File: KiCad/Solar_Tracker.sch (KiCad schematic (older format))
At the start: 127 parts

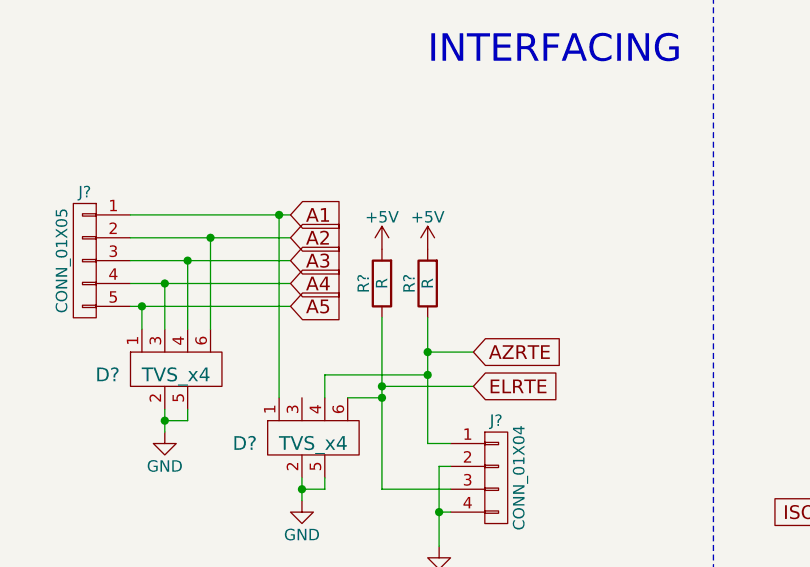
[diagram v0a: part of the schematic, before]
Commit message: Updated pullups on config jumpers
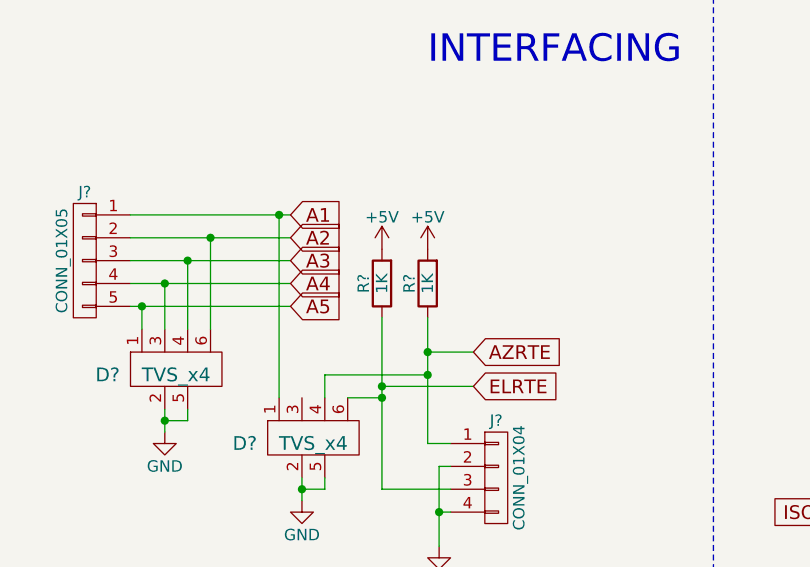
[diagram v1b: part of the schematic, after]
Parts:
- R? (x2): value R -> 1K
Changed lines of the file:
@@
 P 8300 6100
 F 0 "R?" V 8380 6100 50  0000 C CNN
-F 1 "R" V 8300 6100 50  0000 C CNN
+F 1 "1K" V 8300 6100 50  0000 C CNN
 F 2 "" V 8230 6100 50  0001 C CNN
 F 3 "" H 8300 6100 50  0001 C CNN
@@
 P 8500 6100
 F 0 "R?" V 8580 6100 50  0000 C CNN
-F 1 "R" V 8500 6100 50  0000 C CNN
+F 1 "1K" V 8500 6100 50  0000 C CNN
 F 2 "" V 8430 6100 50  0001 C CNN
 F 3 "" H 8500 6100 50  0001 C CNN

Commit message: Annotated
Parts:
- gave numbers to parts that had none: 127

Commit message: Redid analog connector
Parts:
- removed D6: TVS_x4, symbol TVS_x4
- removed J6, J7: CONN_01X04, symbol CONN_01X04
- added D14: TVS_x4, symbol TVS_x4
- added J10, J11, J12, J13: HOLE, symbol CONN_01X01
- added J14: ELJMP, symbol CONN_01X02_MALE
- added J6: GPIO, symbol CONN_01X08
- added J7: AZJMP, symbol CONN_01X02_MALE
- added R44: 150, symbol R
- R15, R26, R43, R7: value R -> 1K
- renumbered D14 to D6
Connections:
- net +5V: now also R44.2
- net A0: now also D7.3, J4.2 (P2)
- net A1: now also J4.3 (P3); no longer J4.1 (P1)
- net A2: now also D14.6, J6.5 (P5); no longer J4.2 (P2)
- net A3: now also D14.4, J6.6 (P6); no longer J4.3 (P3)
- net A4: now also D14.3, J6.7 (P7); no longer J4.4 (P4)
- net A5: now also D14.1, J6.8 (P8); no longer J4.5 (P5)
- net AZRTE: now also J7.1
- net D4: now also J6.1 (P1)
- net D5: now also J6.2 (P2)
- net D6: now also J6.3 (P3)
- net D7: now also J6.4 (P4)
- net ELRTE: now also J14.1
- net Earth: now also C1.2, C10.2, C11.2, C12.2, C13.2, C14.2, C15.2, C16.2, C2.2, C20.2, C21.2, C26.2, C28.2, C29.2, C3.2, C4.2, C6.2, C9.2, D2.3 (GND), D7.2, D7.5, D8.2, D8.5, D9.2, D9.5, J1.2 (Pin_2), J2.5 (GND), J2.6 (Shield), J4.4 (P4), J4.5 (P5), J5.6 (P6), R1.2, R12.2, R18.2, R25.2, R27.2, R32.2, R8.2, R9.2, SW1.~, U1.2 (-Vin), U1.4 (-Vout), U10.2, U12.1 (GND), U12.P (PAD), U2.1 (GND), U2.P (PAD), U3.15 (GND), U3.23 (GND), U3.35 (GND), U3.43 (GND), U3.5 (UGND), U4.1 (GND), U4.P (PAD), U5.1 (GND), U5.P (PAD), U6.2 (-Vin), U7.3, U8.3, U9.2, Y1.2, D14.2, D14.5, J10.1 (P1), J11.1 (P1), J12.1 (P1), J13.1 (P1), J14.2, J7.2
- removed net GND: C1.2, C10.2, C11.2, C12.2, C13.2, C14.2, C15.2, C16.2, C2.2, C20.2, C21.2, C26.2, C28.2, C29.2, C3.2, C4.2, C6.2, C9.2, D2.3 (GND), D7.2, D7.5, D8.2, D8.5, D9.2, D9.5, J1.2 (Pin_2), J2.5 (GND), J2.6 (Shield), J5.6 (P6), R1.2, R12.2, R18.2, R25.2, R27.2, R32.2, R8.2, R9.2, SW1.~, U1.2 (-Vin), U1.4 (-Vout), U10.2, U12.1 (GND), U12.P (PAD), U2.1 (GND), U2.P (PAD), U3.15 (GND), U3.23 (GND), U3.35 (GND), U3.43 (GND), U3.5 (UGND), U4.1 (GND), U4.P (PAD), U5.1 (GND), U5.P (PAD), U6.2 (-Vin), U7.3, U8.3, U9.2, Y1.2
- new net: J4.1 (P1), R44.1
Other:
- note added: "BLK"
- note added: "BRE"
- note added: "GRN"
- note added: "RED"
- note added: "WHT"
- moved on the sheet: D7, D9

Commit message: New motor cap values
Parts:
- C15, C20, C28, C3: value 560nF?? -> 1u
- C16, C17, C21, C22, C29, C31, C4, C5: value 100nF -> 100n
- C18, C23, C33, C7: value 12nF????? -> 0.015u
- C19, C24, C36, C8: value 470nF -> 470n
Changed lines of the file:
@@
 P 14950 3100
 F 0 "C33" H 14960 3170 50  0000 L CNN
-F 1 "12nF?????" H 14850 3050 50  0000 L CNN
+F 1 "0.015u" H 14850 3050 50  0000 L CNN
 F 2 "" H 14950 3100 50  0001 C CNN
 F 3 "" H 14950 3100 50  0001 C CNN
@@
 P 14150 1100
 F 0 "C29" H 14160 1170 50  0000 L CNN
-F 1 "100nF" H 14050 1050 50  0000 L CNN
+F 1 "100n" H 14050 1050 50  0000 L CNN
 F 2 "" H 14150 1100 50  0001 C CNN
 F 3 "" H 14150 1100 50  0001 C CNN
@@
 P 15850 2100
 F 0 "C36" H 15860 2170 50  0000 L CNN
-F 1 "470nF" H 15750 2050 50  0000 L CNN
+F 1 "470n" H 15750 2050 50  0000 L CNN
 F 2 "" H 15850 2100 50  0001 C CNN
 F 3 "" H 15850 2100 50  0001 C CNN
@@
 P 14150 750
 F 0 "C28" H 14160 820 50  0000 L CNN
-F 1 "560nF??" H 14050 700 50  0000 L CNN
+F 1 "1u" H 14050 700 50  0000 L CNN
 F 2 "" H 14150 750 50  0001 C CNN
 F 3 "" H 14150 750 50  0001 C CNN
@@
 P 14400 3300
 F 0 "C31" H 14410 3370 50  0000 L CNN
-F 1 "100nF" H 14410 3220 50  0000 L CNN
+F 1 "100n" H 14410 3220 50  0000 L CNN
 F 2 "" H 14400 3300 50  0001 C CNN
 F 3 "" H 14400 3300 50  0001 C CNN
@@
 P 10900 3100
 F 0 "C23" H 10910 3170 50  0000 L CNN
-F 1 "12nF?????" H 10800 3050 50  0000 L CNN
+F 1 "0.015u" H 10800 3050 50  0000 L CNN
 F 2 "" H 10900 3100 50  0001 C CNN
 F 3 "" H 10900 3100 50  0001 C CNN
@@
 P 10100 1100
 F 0 "C21" H 10110 1170 50  0000 L CNN
-F 1 "100nF" H 10000 1050 50  0000 L CNN
+F 1 "100n" H 10000 1050 50  0000 L CNN
 F 2 "" H 10100 1100 50  0001 C CNN
 F 3 "" H 10100 1100 50  0001 C CNN
@@
 P 11800 2100
 F 0 "C24" H 11810 2170 50  0000 L CNN
-F 1 "470nF" H 11700 2050 50  0000 L CNN
+F 1 "470n" H 11700 2050 50  0000 L CNN
 F 2 "" H 11800 2100 50  0001 C CNN
 F 3 "" H 11800 2100 50  0001 C CNN
@@
 P 10100 750
 F 0 "C20" H 10110 820 50  0000 L CNN
-F 1 "560nF??" H 10000 700 50  0000 L CNN
+F 1 "1u" H 10000 700 50  0000 L CNN
 F 2 "" H 10100 750 50  0001 C CNN
 F 3 "" H 10100 750 50  0001 C CNN
@@
 P 10350 3300
 F 0 "C22" H 10360 3370 50  0000 L CNN
-F 1 "100nF" H 10360 3220 50  0000 L CNN
+F 1 "100n" H 10360 3220 50  0000 L CNN
 F 2 "" H 10350 3300 50  0001 C CNN
 F 3 "" H 10350 3300 50  0001 C CNN
@@
 P 6900 3100
 F 0 "C18" H 6910 3170 50  0000 L CNN
-F 1 "12nF?????" H 6800 3050 50  0000 L CNN
+F 1 "0.015u" H 6800 3050 50  0000 L CNN
 F 2 "" H 6900 3100 50  0001 C CNN
 F 3 "" H 6900 3100 50  0001 C CNN
@@
 P 6100 1100
 F 0 "C16" H 6110 1170 50  0000 L CNN
-F 1 "100nF" H 6000 1050 50  0000 L CNN
+F 1 "100n" H 6000 1050 50  0000 L CNN
 F 2 "" H 6100 1100 50  0001 C CNN
 F 3 "" H 6100 1100 50  0001 C CNN
@@
 P 7800 2100
 F 0 "C19" H 7810 2170 50  0000 L CNN
-F 1 "470nF" H 7700 2050 50  0000 L CNN
+F 1 "470n" H 7700 2050 50  0000 L CNN
 F 2 "" H 7800 2100 50  0001 C CNN
 F 3 "" H 7800 2100 50  0001 C CNN
@@
 P 6100 750
 F 0 "C15" H 6110 820 50  0000 L CNN
-F 1 "560nF??" H 6000 700 50  0000 L CNN
+F 1 "1u" H 6000 700 50  0000 L CNN
 F 2 "" H 6100 750 50  0001 C CNN
 F 3 "" H 6100 750 50  0001 C CNN
@@
 P 6350 3300
 F 0 "C17" H 6360 3370 50  0000 L CNN
-F 1 "100nF" H 6360 3220 50  0000 L CNN
+F 1 "100n" H 6360 3220 50  0000 L CNN
 F 2 "" H 6350 3300 50  0001 C CNN
 F 3 "" H 6350 3300 50  0001 C CNN
@@
 P 2900 3100
 F 0 "C7" H 2910 3170 50  0000 L CNN
-F 1 "12nF?????" H 2800 3050 50  0000 L CNN
+F 1 "0.015u" H 2800 3050 50  0000 L CNN
 F 2 "" H 2900 3100 50  0001 C CNN
 F 3 "" H 2900 3100 50  0001 C CNN
@@
 P 2100 1100
 F 0 "C4" H 2110 1170 50  0000 L CNN
-F 1 "100nF" H 2000 1050 50  0000 L CNN
+F 1 "100n" H 2000 1050 50  0000 L CNN
 F 2 "" H 2100 1100 50  0001 C CNN
 F 3 "" H 2100 1100 50  0001 C CNN
@@
 P 3800 2100
 F 0 "C8" H 3810 2170 50  0000 L CNN
-F 1 "470nF" H 3700 2050 50  0000 L CNN
+F 1 "470n" H 3700 2050 50  0000 L CNN
 F 2 "" H 3800 2100 50  0001 C CNN
 F 3 "" H 3800 2100 50  0001 C CNN
@@
 P 2100 750
 F 0 "C3" H 2110 820 50  0000 L CNN
-F 1 "560nF??" H 2000 700 50  0000 L CNN
+F 1 "1u" H 2000 700 50  0000 L CNN
 F 2 "" H 2100 750 50  0001 C CNN
 F 3 "" H 2100 750 50  0001 C CNN
@@
 P 2350 3300
 F 0 "C5" H 2360 3370 50  0000 L CNN
-F 1 "100nF" H 2360 3220 50  0000 L CNN
+F 1 "100n" H 2360 3220 50  0000 L CNN
 F 2 "" H 2350 3300 50  0001 C CNN
 F 3 "" H 2350 3300 50  0001 C CNN

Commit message: Paired with footprints
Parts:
- removed C26, C9: 6800u, symbol C
- added C26, C9: 6800u, Capacitors_THT:CP_Radial_D22.0mm_P10.00mm_SnapIn, symbol CP
- C1, C10, C11, C12, C13, C14, C15, C16, C17, C18, C19, C2, C20, C21, C22, C23, C24, C25, C27, C28, C29, C3, C30, C31, C32, C33, C34, C35, C36, C4, C5, C6, C7, C8: footprint (none) -> Capacitors_SMD:C_1206_HandSoldering
- D1, D10, D11, D12, D13, D3, D4, D5, D6: footprint (none) -> LEDs:LED_1206_HandSoldering
- D15: footprint (none) -> TO_SOT_Packages_SMD:SOT-23
- J2: footprint (none) -> Connectors:USB_Micro-B
- L1, L2: footprint (none) -> Inductors_SMD:L_1206_HandSoldering
- R1, R10, R11, R12, R13, R14, R15, R16, R17, R18, R19, R2, R20, R21, R22, R23, R24, R25, R26, R27, R28, R29, R3, R30, R31, R32, R33, R34, R35, R36, R37, R38, R39, R4, R40, R41, R42, R43, R44, R5, R6, R7, R8, R9: footprint (none) -> Resistors_SMD:R_1206_HandSoldering
- U11: footprint (none) -> Housings_DIP:DIP-8_W7.62mm
- U12, U2, U4, U5: footprint (none) -> Housings_SSOP:ST_PowerSSO-24_SlugDown_ThermalVias
- U3: footprint TQFP44 -> Housings_QFP:TQFP-44_10x10mm_Pitch0.8mm
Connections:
- net +48V: now also C26.1, C9.1
- net Earth: now also C26.2, C9.2

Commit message: Added nFET footprint
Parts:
- J1, J3, J8: footprint (none) -> Connectors_Phoenix:PhoenixContact_GMSTBA-G_02x7.50mm_Angled
- J14: footprint (none) -> Pin_Headers:Pin_Header_Angled_1x02_Pitch2.54mm
- J4: footprint (none) -> Connectors_Phoenix:PhoenixContact_GMSTBA-G_05x7.50mm_Angled
- J5: footprint (none) -> Pin_Headers:Pin_Header_Straight_2x03_Pitch2.54mm
- J6: footprint (none) -> Connectors_Phoenix:PhoenixContact_GMSTBA-G_08x7.50mm_Angled
- J7: footprint (none) -> Pin_Headers:Pin_Header_Straight_1x02_Pitch2.54mm
- J9: footprint (none) -> Connectors_Phoenix:PhoenixContact_GMSTBA-G_03x7.50mm_Angled
- Q1, Q2, Q3, Q4, Q5, Q6, Q7, Q8: footprint (none) -> Solar:nFET
- SW1: footprint (none) -> Buttons_Switches_SMD:SW_SPST_B3S-1000
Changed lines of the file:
@@
 F 0 "J5" H 8100 8150 50  0000 C CNN
 F 1 "CONN_02X03" H 8100 7750 50  0000 C CNN
-F 2 "" H 8100 6750 50  0001 C CNN
+F 2 "Pin_Headers:Pin_Header_Straight_2x03_Pitch2.54mm" H 8100 6750 50  0001 C CNN
 F 3 "" H 8100 6750 50  0001 C CNN
 	1    8100 7950
@@
 F 0 "J9" H 16100 8050 50  0000 C CNN
 F 1 "CONN_01X03" V 16200 7850 50  0000 C CNN
-F 2 "" H 16100 7850 50  0001 C CNN
+F 2 "Connectors_Phoenix:PhoenixContact_GMSTBA-G_03x7.50mm_Angled" H 16100 7850 50  0001 C CNN
 F 3 "" H 16100 7850 50  0001 C CNN
 	1    16100 7850
@@
 F 0 "SW1" H 1050 7250 60  0000 C CNN
 F 1 "SWITCH" H 1050 7100 60  0000 C CNN
-F 2 "" H 1050 7150 60  0001 C CNN
+F 2 "Buttons_Switches_SMD:SW_SPST_B3S-1000" H 1050 7150 60  0001 C CNN
 F 3 "" H 1050 7150 60  0001 C CNN
 	1    1050 7150
@@
 F 0 "J4" H 7000 6300 50  0000 C CNN
 F 1 "CONN_01X05" V 7100 6000 50  0000 C CNN
-F 2 "" H 7000 6000 50  0001 C CNN
+F 2 "Connectors_Phoenix:PhoenixContact_GMSTBA-G_05x7.50mm_Angled" H 7000 6000 50  0001 C CNN
 F 3 "" H 7000 6000 50  0001 C CNN
 	1    7000 6000
@@
 F 0 "J3" H 4250 3750 50  0000 C CNN
 F 1 "EL" V 4350 3600 50  0000 C CNN
-F 2 "" H 4250 3600 50  0001 C CNN
+F 2 "Connectors_Phoenix:PhoenixContact_GMSTBA-G_02x7.50mm_Angled" H 4250 3600 50  0001 C CNN
 F 3 "" H 4250 3600 50  0001 C CNN
 	1    4250 3600
@@
 F 0 "J8" H 12300 3800 50  0000 C CNN
 F 1 "AZ" V 12400 3650 50  0000 C CNN
-F 2 "" H 12300 3650 50  0001 C CNN
+F 2 "Connectors_Phoenix:PhoenixContact_GMSTBA-G_02x7.50mm_Angled" H 12300 3650 50  0001 C CNN
 F 3 "" H 12300 3650 50  0001 C CNN
 	1    12300 3650
@@
 F 0 "Q8" H 15450 3950 60  0000 C CNN
 F 1 "BUK9M42-60E" H 15600 3550 60  0000 C CNN
-F 2 "" V 15300 3450 60  0001 C CNN
+F 2 "Solar:nFET" V 15300 3450 60  0001 C CNN
 F 3 "" V 15300 3450 60  0001 C CNN
 	1    15250 3750
@@
 F 0 "Q7" H 14250 3950 60  0000 C CNN
 F 1 "BUK9M42-60E" H 14400 3550 60  0000 C CNN
-F 2 "" V 14100 3450 60  0001 C CNN
+F 2 "Solar:nFET" V 14100 3450 60  0001 C CNN
 F 3 "" V 14100 3450 60  0001 C CNN
 	1    14050 3750
@@
 F 0 "Q6" H 11400 3950 60  0000 C CNN
 F 1 "BUK9M42-60E" H 11550 3550 60  0000 C CNN
-F 2 "" V 11250 3450 60  0001 C CNN
+F 2 "Solar:nFET" V 11250 3450 60  0001 C CNN
 F 3 "" V 11250 3450 60  0001 C CNN
 	1    11200 3750
@@
 F 0 "Q5" H 10200 3950 60  0000 C CNN
 F 1 "BUK9M42-60E" H 10350 3550 60  0000 C CNN
-F 2 "" V 10050 3450 60  0001 C CNN
+F 2 "Solar:nFET" V 10050 3450 60  0001 C CNN
 F 3 "" V 10050 3450 60  0001 C CNN
 	1    10000 3750
@@
 F 0 "Q4" H 7400 3950 60  0000 C CNN
 F 1 "BUK9M42-60E" H 7550 3550 60  0000 C CNN
-F 2 "" V 7250 3450 60  0001 C CNN
+F 2 "Solar:nFET" V 7250 3450 60  0001 C CNN
 F 3 "" V 7250 3450 60  0001 C CNN
 	1    7200 3750
@@
 F 0 "Q3" H 6200 3950 60  0000 C CNN
 F 1 "BUK9M42-60E" H 6350 3550 60  0000 C CNN
-F 2 "" V 6050 3450 60  0001 C CNN
+F 2 "Solar:nFET" V 6050 3450 60  0001 C CNN
 F 3 "" V 6050 3450 60  0001 C CNN
 	1    6000 3750
@@
 F 0 "Q2" H 3400 3950 60  0000 C CNN
 F 1 "BUK9M42-60E" H 3550 3550 60  0000 C CNN
-F 2 "" V 3250 3450 60  0001 C CNN
+F 2 "Solar:nFET" V 3250 3450 60  0001 C CNN
 F 3 "" V 3250 3450 60  0001 C CNN
 	1    3200 3750
@@
 F 0 "Q1" H 2200 3950 60  0000 C CNN
 F 1 "BUK9M42-60E" H 2350 3550 60  0000 C CNN
-F 2 "" V 2050 3450 60  0001 C CNN
+F 2 "Solar:nFET" V 2050 3450 60  0001 C CNN
 F 3 "" V 2050 3450 60  0001 C CNN
 	1    2000 3750
@@
 F 0 "J1" H 900 5200 50  0000 C CNN
 F 1 "+48V_IN" H 900 4900 50  0000 C CNN
-F 2 "" H 900 5100 50  0001 C CNN
+F 2 "Connectors_Phoenix:PhoenixContact_GMSTBA-G_02x7.50mm_Angled" H 900 5100 50  0001 C CNN
 F 3 "" H 900 5100 50  0001 C CNN
 	1    900  5100
@@
 F 0 "J7" H 9350 7025 50  0000 C CNN
 F 1 "AZJMP" H 9350 6650 50  0000 C CNN
-F 2 "" H 9350 6950 50  0001 C CNN
+F 2 "Pin_Headers:Pin_Header_Straight_1x02_Pitch2.54mm" H 9350 6950 50  0001 C CNN
 F 3 "" H 9350 6950 50  0001 C CNN
 	1    9350 6850
@@
 F 0 "J14" H 9350 7475 50  0000 C CNN
 F 1 "ELJMP" H 9350 7100 50  0000 C CNN
-F 2 "" H 9350 7400 50  0001 C CNN
+F 2 "Pin_Headers:Pin_Header_Angled_1x02_Pitch2.54mm" H 9350 7400 50  0001 C CNN
 F 3 "" H 9350 7400 50  0001 C CNN
 	1    9350 7300
@@
 F 0 "J6" H 8700 10000 50  0000 C CNN
 F 1 "GPIO" V 8800 9550 50  0000 C CNN
-F 2 "" H 8700 9550 50  0001 C CNN
+F 2 "Connectors_Phoenix:PhoenixContact_GMSTBA-G_08x7.50mm_Angled" H 8700 9550 50  0001 C CNN
 F 3 "" H 8700 9550 50  0001 C CNN
 	1    8700 9550

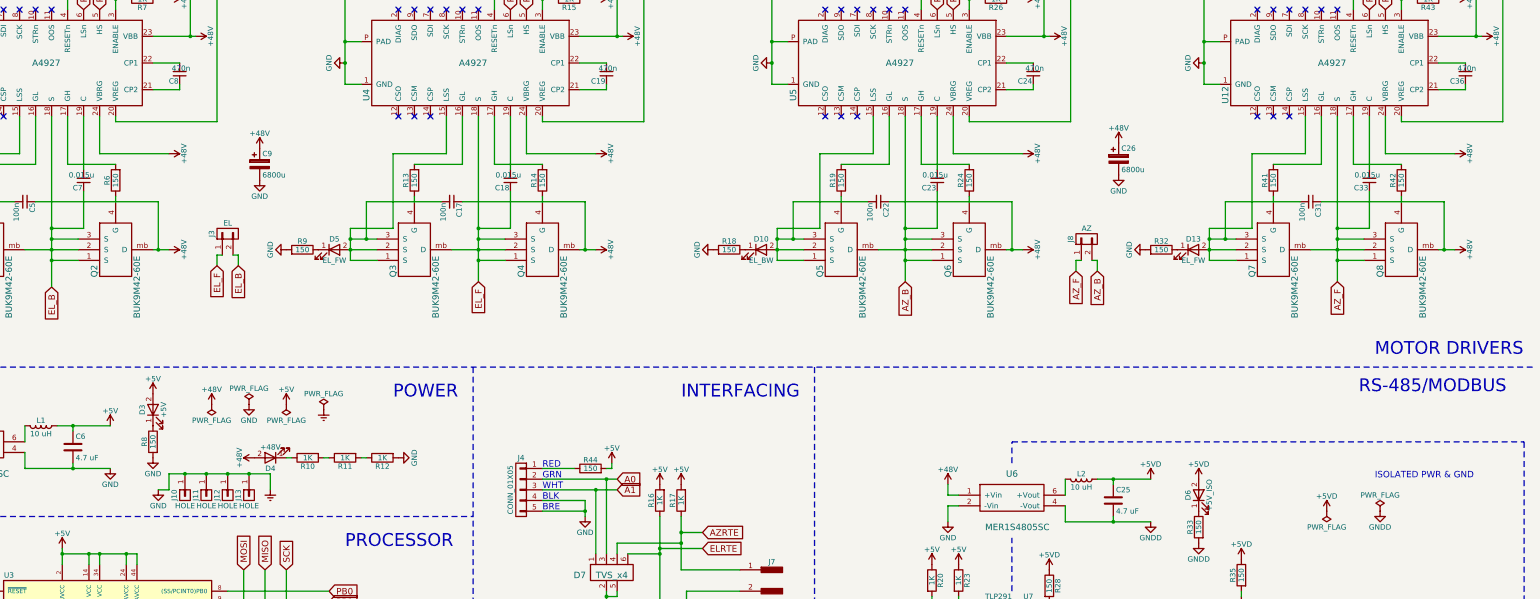
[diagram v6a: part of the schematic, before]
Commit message: Changed 5v filter caps
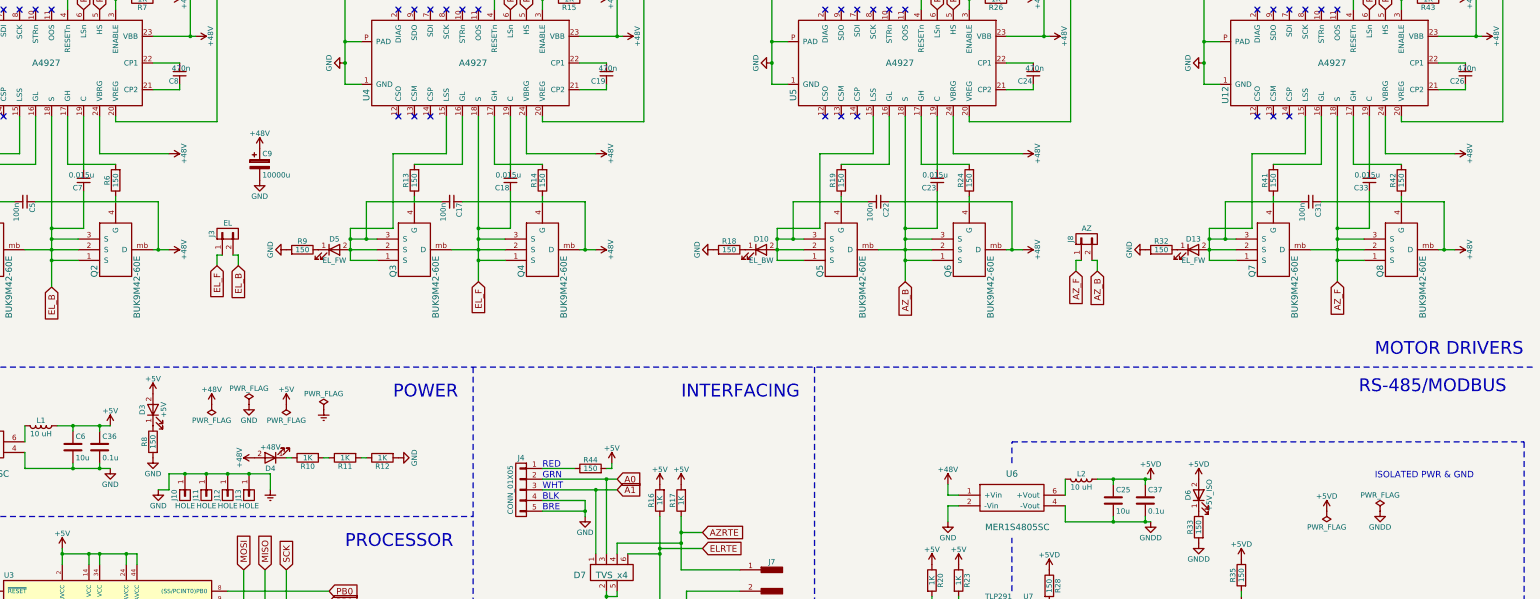
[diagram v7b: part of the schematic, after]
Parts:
- removed C26: 6800u, Capacitors_THT:CP_Radial_D22.0mm_P10.00mm_SnapIn, symbol CP
- added C36, C37: 0.1u, Capacitors_SMD:C_1206_HandSoldering, symbol C
- C25, C6: value 4.7 uF -> 10u
- C9: value 6800u -> 10000u
- renumbered C36 to C26
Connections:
- net +5V: now also C36.1
- net +5VD: now also C37.1
- net Earth: now also C36.2
- net GNDD: now also C37.2

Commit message: Associated footprints
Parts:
- C16, C21, C29, C4: value 100n -> 0.1u
- C19, C24, C26, C8: value 470n -> 0.47u
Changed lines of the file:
@@
 P 14150 1100
 F 0 "C29" H 14160 1170 50  0000 L CNN
-F 1 "100n" H 14050 1050 50  0000 L CNN
+F 1 "0.1u" H 14050 1050 50  0000 L CNN
 F 2 "Capacitors_SMD:C_1206_HandSoldering" H 14150 1100 50  0001 C CNN
 F 3 "" H 14150 1100 50  0001 C CNN
@@
 P 15850 2100
 F 0 "C26" H 15860 2170 50  0000 L CNN
-F 1 "470n" H 15750 2050 50  0000 L CNN
+F 1 "0.47u" H 15750 2050 50  0000 L CNN
 F 2 "Capacitors_SMD:C_1206_HandSoldering" H 15850 2100 50  0001 C CNN
 F 3 "" H 15850 2100 50  0001 C CNN
@@
 P 10100 1100
 F 0 "C21" H 10110 1170 50  0000 L CNN
-F 1 "100n" H 10000 1050 50  0000 L CNN
+F 1 "0.1u" H 10000 1050 50  0000 L CNN
 F 2 "Capacitors_SMD:C_1206_HandSoldering" H 10100 1100 50  0001 C CNN
 F 3 "" H 10100 1100 50  0001 C CNN
@@
 P 11800 2100
 F 0 "C24" H 11810 2170 50  0000 L CNN
-F 1 "470n" H 11700 2050 50  0000 L CNN
+F 1 "0.47u" H 11700 2050 50  0000 L CNN
 F 2 "Capacitors_SMD:C_1206_HandSoldering" H 11800 2100 50  0001 C CNN
 F 3 "" H 11800 2100 50  0001 C CNN
@@
 P 6100 1100
 F 0 "C16" H 6110 1170 50  0000 L CNN
-F 1 "100n" H 6000 1050 50  0000 L CNN
+F 1 "0.1u" H 6000 1050 50  0000 L CNN
 F 2 "Capacitors_SMD:C_1206_HandSoldering" H 6100 1100 50  0001 C CNN
 F 3 "" H 6100 1100 50  0001 C CNN
@@
 P 7800 2100
 F 0 "C19" H 7810 2170 50  0000 L CNN
-F 1 "470n" H 7700 2050 50  0000 L CNN
+F 1 "0.47u" H 7700 2050 50  0000 L CNN
 F 2 "Capacitors_SMD:C_1206_HandSoldering" H 7800 2100 50  0001 C CNN
 F 3 "" H 7800 2100 50  0001 C CNN
@@
 P 2100 1100
 F 0 "C4" H 2110 1170 50  0000 L CNN
-F 1 "100n" H 2000 1050 50  0000 L CNN
+F 1 "0.1u" H 2000 1050 50  0000 L CNN
 F 2 "Capacitors_SMD:C_1206_HandSoldering" H 2100 1100 50  0001 C CNN
 F 3 "" H 2100 1100 50  0001 C CNN
@@
 P 3800 2100
 F 0 "C8" H 3810 2170 50  0000 L CNN
-F 1 "470n" H 3700 2050 50  0000 L CNN
+F 1 "0.47u" H 3700 2050 50  0000 L CNN
 F 2 "Capacitors_SMD:C_1206_HandSoldering" H 3800 2100 50  0001 C CNN
 F 3 "" H 3800 2100 50  0001 C CNN
